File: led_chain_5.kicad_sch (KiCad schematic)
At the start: 0 parts

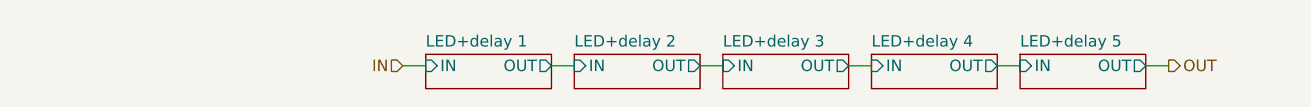
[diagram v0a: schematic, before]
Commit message: pcb-text plugin applied, next step is to write a replicate layout plugin that actually works
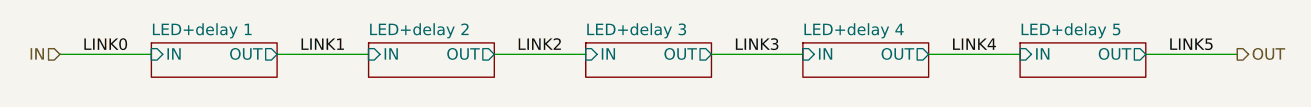
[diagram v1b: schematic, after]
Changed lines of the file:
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@@
 (kicad_sch (version 20211123) (generator eeschema)
   (paper "A4")
-  (wire (pts (xy 175.26 157.48) (xy 177.8 157.48))
+  (wire (pts (xy 144.78 156.21) (xy 154.94 156.21))
     (stroke (width 0) (type default) (color 0 0 0 0))
   )
-  (wire (pts (xy 158.75 157.48) (xy 161.29 157.48))
+  (wire (pts (xy 120.65 156.21) (xy 130.81 156.21))
     (stroke (width 0) (type default) (color 0 0 0 0))
   )
-  (wire (pts (xy 224.79 157.48) (xy 227.33 157.48))
+  (wire (pts (xy 217.17 156.21) (xy 227.33 156.21))
     (stroke (width 0) (type default) (color 0 0 0 0))
   )
-  (wire (pts (xy 241.3 157.48) (xy 243.84 157.48))
+  (wire (pts (xy 241.3 156.21) (xy 251.46 156.21))
     (stroke (width 0) (type default) (color 0 0 0 0))
   )
-  (wire (pts (xy 191.77 157.48) (xy 194.31 157.48))
+  (wire (pts (xy 168.91 156.21) (xy 179.07 156.21))
     (stroke (width 0) (type default) (color 0 0 0 0))
   )
-  (wire (pts (xy 208.28 157.48) (xy 210.82 157.48))
+  (wire (pts (xy 193.04 156.21) (xy 203.2 156.21))
     (stroke (width 0) (type default) (color 0 0 0 0))
   )
-  (hierarchical_label "IN" (shape input) (at 158.75 157.48 180)
+  (label "LINK0" (at 123.19 156.21 0)
+    (effects (font (size 1.27 1.27)) (justify left bottom))
+  )
+  (label "LINK2" (at 171.45 156.21 0)
+    (effects (font (size 1.27 1.27)) (justify left bottom))
+  )
+  (label "LINK1" (at 147.32 156.21 0)
+    (effects (font (size 1.27 1.27)) (justify left bottom))
+  )
+  (label "LINK3" (at 195.58 156.21 0)
+    (effects (font (size 1.27 1.27)) (justify left bottom))
+  )
+  (label "LINK4" (at 219.71 156.21 0)
+    (effects (font (size 1.27 1.27)) (justify left bottom))
+  )
+  (label "LINK5" (at 243.84 156.21 0)
+    (effects (font (size 1.27 1.27)) (justify left bottom))
+  )
+  (hierarchical_label "IN" (shape input) (at 120.65 156.21 180)
     (effects (font (size 1.27 1.27)) (justify right))
   )
-  (hierarchical_label "OUT" (shape output) (at 243.84 157.48 0)
+  (hierarchical_label "OUT" (shape output) (at 251.46 156.21 0)
     (effects (font (size 1.27 1.27)) (justify left))
   )
-  (sheet (at 161.29 156.21) (size 13.97 3.81) (fields_autoplaced)
+  (sheet (at 130.81 154.94) (size 13.97 3.81) (fields_autoplaced)
     (stroke (width 0.1524) (type solid) (color 0 0 0 0))
     (fill (color 0 0 0 0.0000))
-    (property "Sheet name" "LED+delay 1" (id 0) (at 161.29 155.4984 0)
+    (property "Sheet name" "LED+delay 1" (id 0) (at 130.81 154.2284 0)
       (effects (font (size 1.27 1.27)) (justify left bottom))
     )
-    (property "Sheet file" "led_chain_delay_link.kicad_sch" (id 1) (at 161.29 160.6046 0)
+    (property "Sheet file" "led_chain_delay_link.kicad_sch" (id 1) (at 130.81 159.3346 0)
       (effects (font (size 1.27 1.27)) (justify left top) hide)
     )
-    (pin "IN" input (at 161.29 157.48 180)
+    (pin "IN" input (at 130.81 156.21 180)
       (effects (font (size 1.27 1.27)) (justify left))
     )
-    (pin "OUT" output (at 175.26 157.48 0)
+    (pin "OUT" output (at 144.78 156.21 0)
       (effects (font (size 1.27 1.27)) (justify right))
     )
   )
-  (sheet (at 227.33 156.21) (size 13.97 3.81) (fields_autoplaced)
+  (sheet (at 227.33 154.94) (size 13.97 3.81) (fields_autoplaced)
     (stroke (width 0.1524) (type solid) (color 0 0 0 0))
     (fill (color 0 0 0 0.0000))
-    (property "Sheet name" "LED+delay 5" (id 0) (at 227.33 155.4984 0)
+    (property "Sheet name" "LED+delay 5" (id 0) (at 227.33 154.2284 0)
       (effects (font (size 1.27 1.27)) (justify left bottom))
     )
-    (property "Sheet file" "led_chain_delay_link.kicad_sch" (id 1) (at 227.33 160.6046 0)
+    (property "Sheet file" "led_chain_delay_link.kicad_sch" (id 1) (at 227.33 159.3346 0)
       (effects (font (size 1.27 1.27)) (justify left top) hide)
     )
-    (pin "IN" input (at 227.33 157.48 180)
+    (pin "IN" input (at 227.33 156.21 180)
       (effects (font (size 1.27 1.27)) (justify left))
     )
-    (pin "OUT" output (at 241.3 157.48 0)
+    (pin "OUT" output (at 241.3 156.21 0)
       (effects (font (size 1.27 1.27)) (justify right))
     )
   )
-  (sheet (at 177.8 156.21) (size 13.97 3.81) (fields_autoplaced)
+  (sheet (at 154.94 154.94) (size 13.97 3.81) (fields_autoplaced)
     (stroke (width 0.1524) (type solid) (color 0 0 0 0))
     (fill (color 0 0 0 0.0000))
-    (property "Sheet name" "LED+delay 2" (id 0) (at 177.8 155.4984 0)
+    (property "Sheet name" "LED+delay 2" (id 0) (at 154.94 154.2284 0)
       (effects (font (size 1.27 1.27)) (justify left bottom))
     )
-    (property "Sheet file" "led_chain_delay_link.kicad_sch" (id 1) (at 177.8 160.6046 0)
+    (property "Sheet file" "led_chain_delay_link.kicad_sch" (id 1) (at 154.94 159.3346 0)
       (effects (font (size 1.27 1.27)) (justify left top) hide)
     )
-    (pin "IN" input (at 177.8 157.48 180)
+    (pin "IN" input (at 154.94 156.21 180)
       (effects (font (size 1.27 1.27)) (justify left))
     )
-    (pin "OUT" output (at 191.77 157.48 0)
+    (pin "OUT" output (at 168.91 156.21 0)
       (effects (font (size 1.27 1.27)) (justify right))
     )
   )
-  (sheet (at 210.82 156.21) (size 13.97 3.81) (fields_autoplaced)
+  (sheet (at 203.2 154.94) (size 13.97 3.81) (fields_autoplaced)
     (stroke (width 0.1524) (type solid) (color 0 0 0 0))
     (fill (color 0 0 0 0.0000))
-    (property "Sheet name" "LED+delay 4" (id 0) (at 210.82 155.4984 0)
+    (property "Sheet name" "LED+delay 4" (id 0) (at 203.2 154.2284 0)
       (effects (font (size 1.27 1.27)) (justify left bottom))
     )
-    (property "Sheet file" "led_chain_delay_link.kicad_sch" (id 1) (at 210.82 160.6046 0)
+    (property "Sheet file" "led_chain_delay_link.kicad_sch" (id 1) (at 203.2 159.3346 0)
       (effects (font (size 1.27 1.27)) (justify left top) hide)
     )
-    (pin "IN" input (at 210.82 157.48 180)
+    (pin "IN" input (at 203.2 156.21 180)
       (effects (font (size 1.27 1.27)) (justify left))
     )
-    (pin "OUT" output (at 224.79 157.48 0)
+    (pin "OUT" output (at 217.17 156.21 0)
       (effects (font (size 1.27 1.27)) (justify right))
     )
   )
-  (sheet (at 194.31 156.21) (size 13.97 3.81) (fields_autoplaced)
+  (sheet (at 179.07 154.94) (size 13.97 3.81) (fields_autoplaced)
     (stroke (width 0.1524) (type solid) (color 0 0 0 0))
     (fill (color 0 0 0 0.0000))
-    (property "Sheet name" "LED+delay 3" (id 0) (at 194.31 155.4984 0)
+    (property "Sheet name" "LED+delay 3" (id 0) (at 179.07 154.2284 0)
       (effects (font (size 1.27 1.27)) (justify left bottom))
     )
-    (property "Sheet file" "led_chain_delay_link.kicad_sch" (id 1) (at 194.31 160.6046 0)
+    (property "Sheet file" "led_chain_delay_link.kicad_sch" (id 1) (at 179.07 159.3346 0)
       (effects (font (size 1.27 1.27)) (justify left top) hide)
     )
-    (pin "IN" input (at 194.31 157.48 180)
+    (pin "IN" input (at 179.07 156.21 180)
       (effects (font (size 1.27 1.27)) (justify left))
     )
-    (pin "OUT" output (at 208.28 157.48 0)
+    (pin "OUT" output (at 193.04 156.21 0)
       (effects (font (size 1.27 1.27)) (justify right))
     )
